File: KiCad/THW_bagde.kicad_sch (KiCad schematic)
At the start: 42 parts, among them J1 USB_B, J2 ISP, SW1 SW_Push, SW2 SW_Push, SW3 SW_Push, U1 ATmega328-P, Y1 Crystal

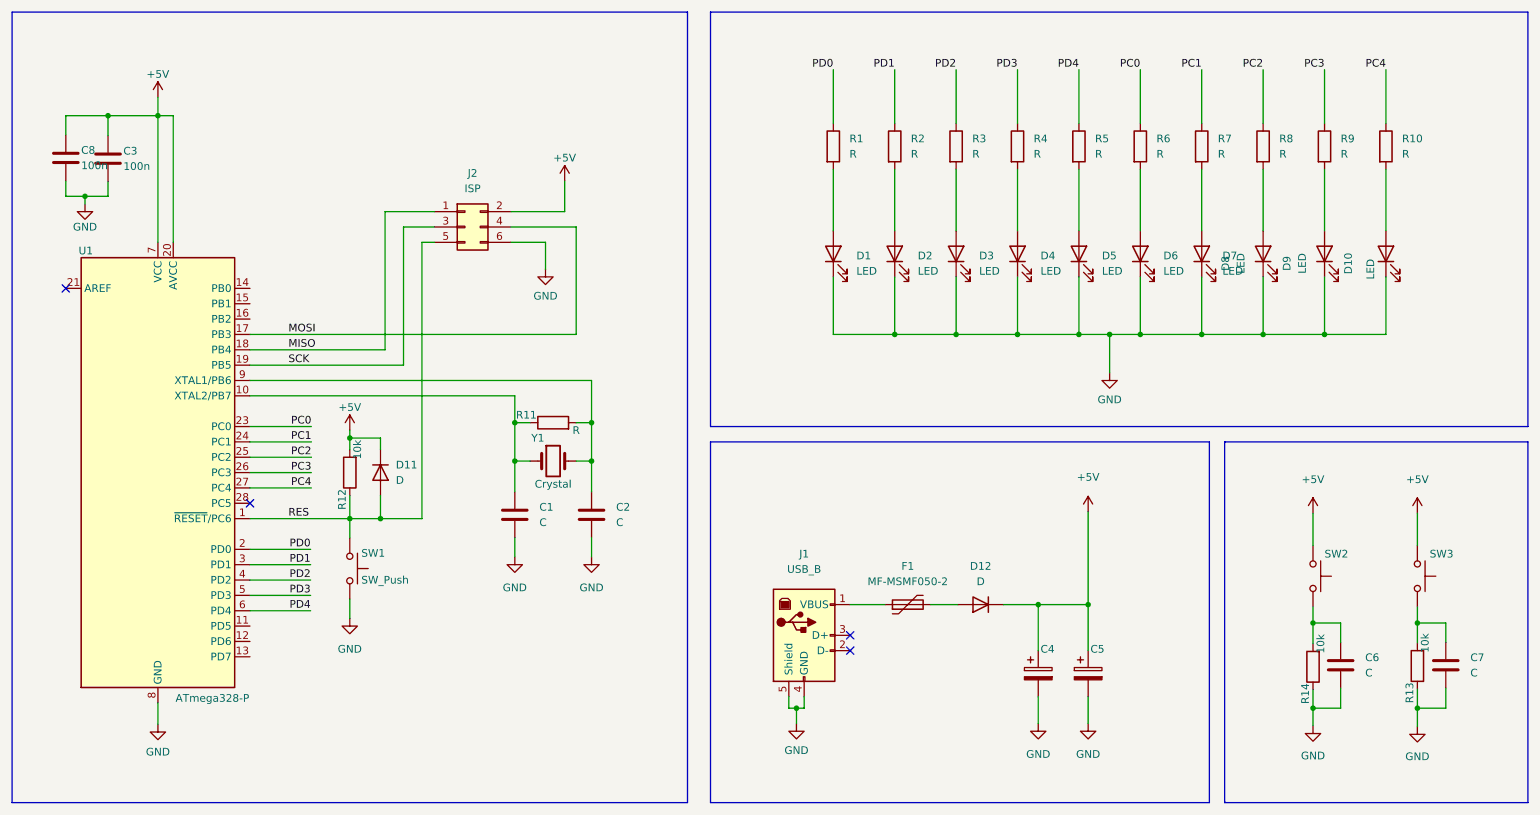
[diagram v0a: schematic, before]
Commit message: fixing pin mapping
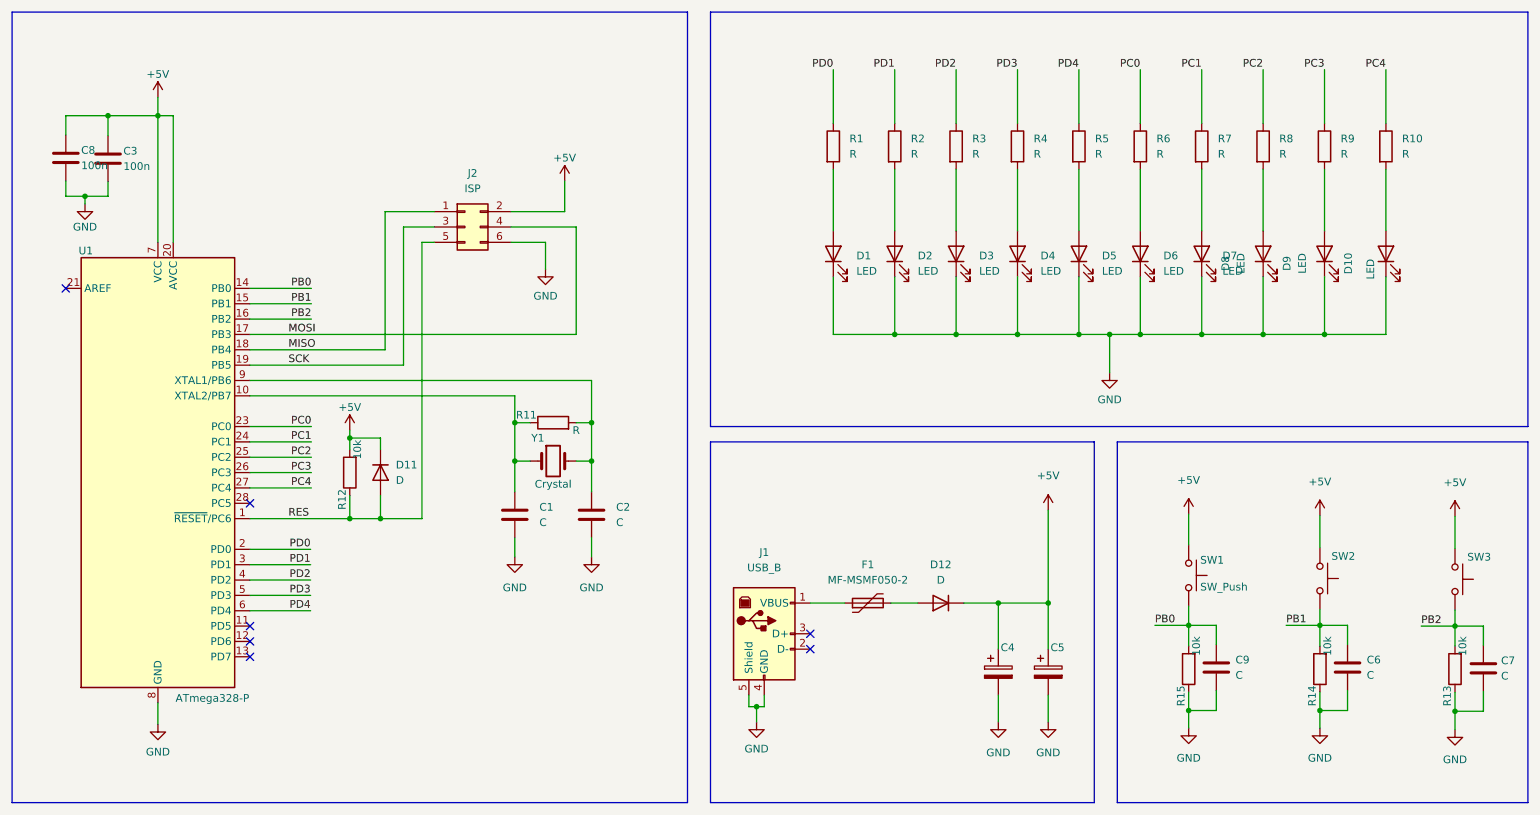
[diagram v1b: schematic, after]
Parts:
- added C9: C, Capacitor_THT:C_Disc_D3.8mm_W2.6mm_P2.50mm, symbol Device:C
- added R15: 10k, Resistor_THT:R_Axial_DIN0207_L6.3mm_D2.5mm_P10.16mm_Horizontal, symbol Device:R
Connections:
- net +5V: now also SW1.1
- net GND: now also C9.2, R15.1; no longer SW1.2
- net RES: no longer SW1.1
- net PB1: now reaches C6.1, R14.2, SW2.2
- net PB1: now also U1.15 (PB1)
- net PB2: now reaches C7.1, R13.2, SW3.2
- net PB2: now also U1.16 (PB2)
- net PB0: now reaches U1.14 (PB0)
- net PB0: now also SW1.2, C9.1, R15.2
- no-connect marks 4 -> 7
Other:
- moved on the sheet: C4, C5, C6, C7, D12, F1, J1, R13, R14, SW1, SW2, SW3

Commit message: Changing  user button circuit. Routing first components. Resize LUG logo in Drawing sheet.
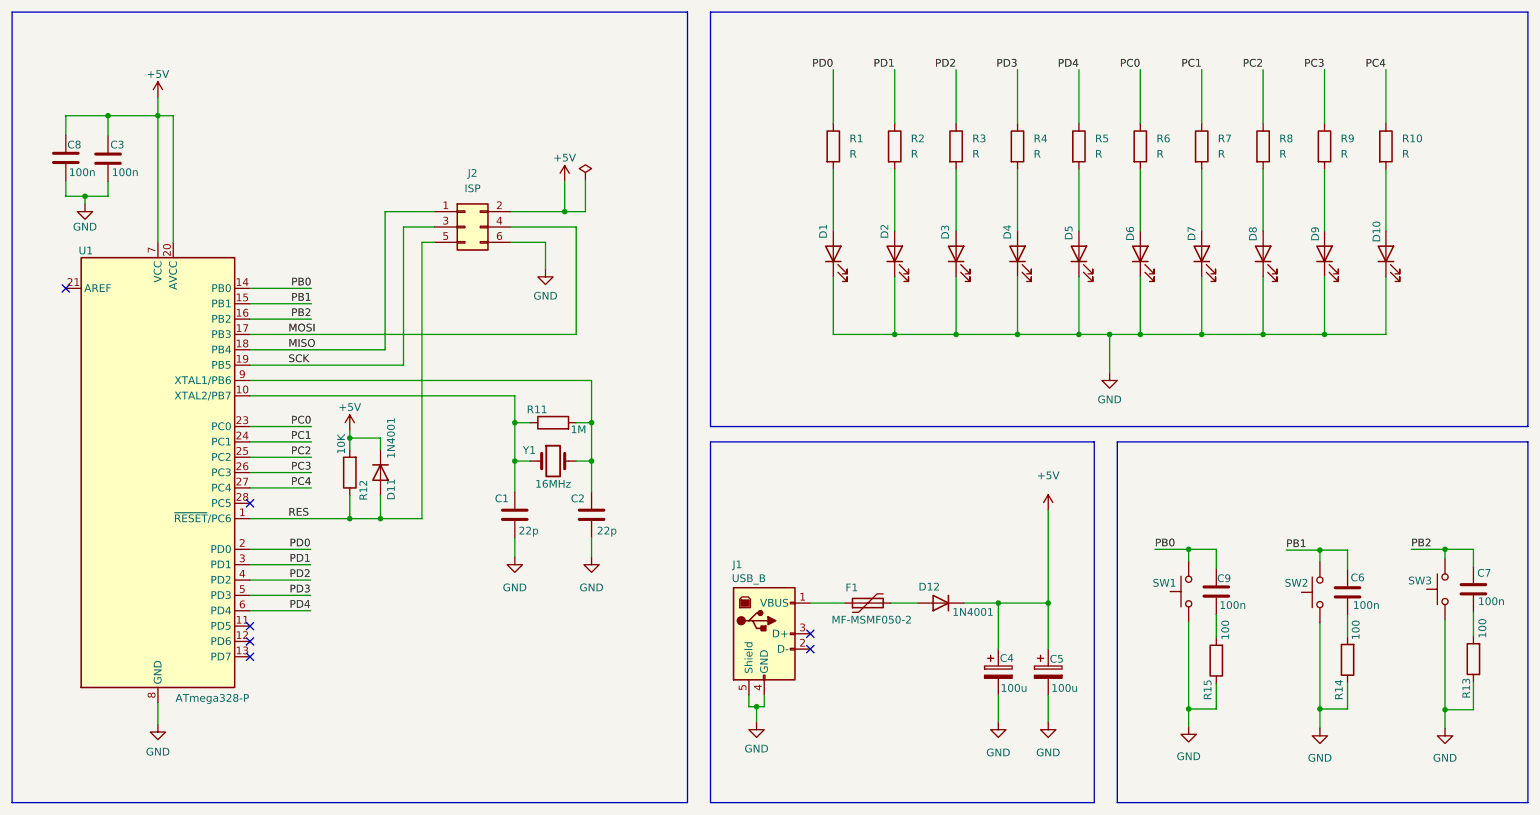
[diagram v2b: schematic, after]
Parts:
- C1, C2: value C -> 22p
- C4, C5: value C_Polarized -> 100u
- C6, C7, C9: value C -> 100n
- D11, D12: value D -> 1N4001
- R11: value R -> 1M
- R12: value 10k -> 10K
- R13, R14, R15: value 10k -> 100
- Y1: value Crystal -> 16MHz
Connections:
- net +5V: no longer SW1.1, SW2.1, SW3.1
- net GND: now also SW1.1, SW2.1, SW3.1; no longer C6.2, C7.2, C9.2
- net PB0: no longer R15.2
- net PB1: no longer R14.2
- net PB2: no longer R13.2
- new net: C9.2, R15.2
- new net: C6.2, R14.2
- new net: C7.2, R13.2
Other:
- company: (none) -> Copyright © Linux User Group Saar e.V.
- title: (none) -> THW-Jugend Badge
- moved on the sheet: C6, C7, C9, R13, R14, R15, SW1, SW2, SW3
